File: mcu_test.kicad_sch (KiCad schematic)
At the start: 3 parts

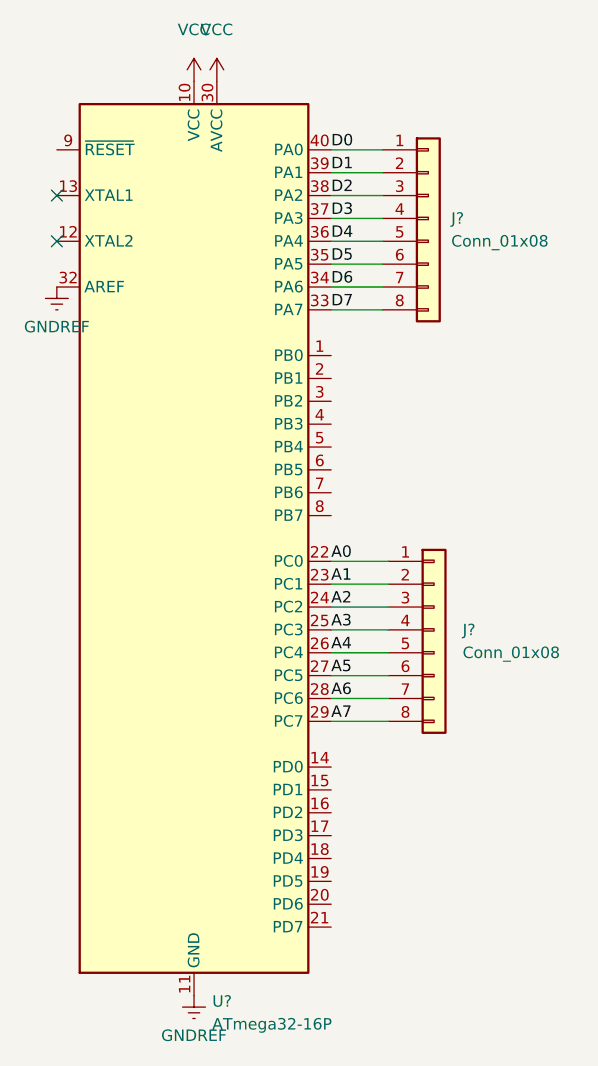
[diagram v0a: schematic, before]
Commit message: Updated to version 8
Changed to version 8; added 96-pin connectors; described ports at PPI_Settings
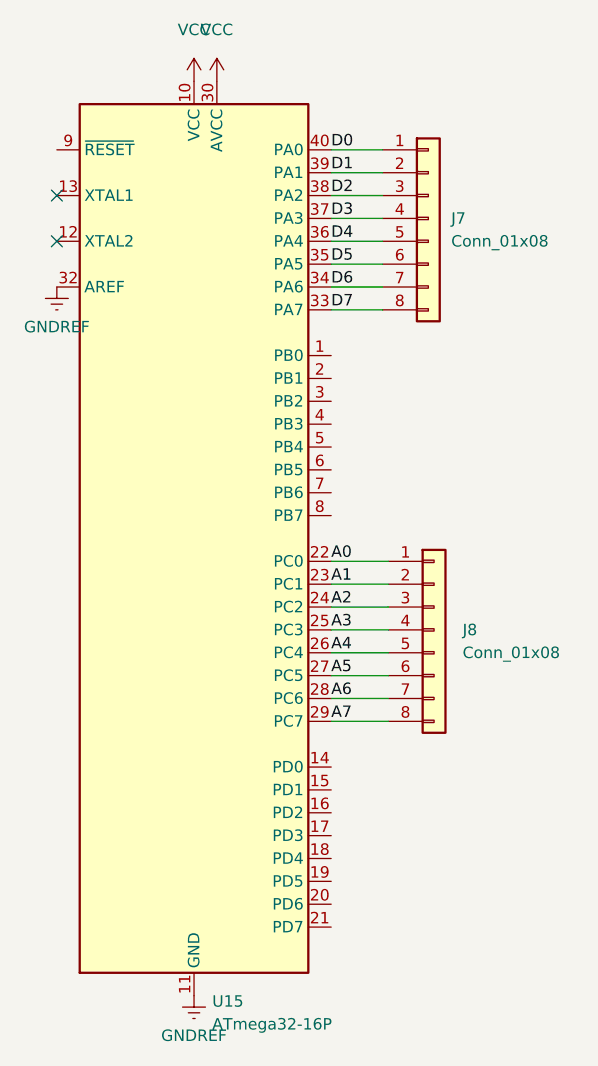
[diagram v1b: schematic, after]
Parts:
- gave numbers to parts that had none: 3
